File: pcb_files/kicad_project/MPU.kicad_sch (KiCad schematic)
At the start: 4 parts, among them U5 MPU-6500

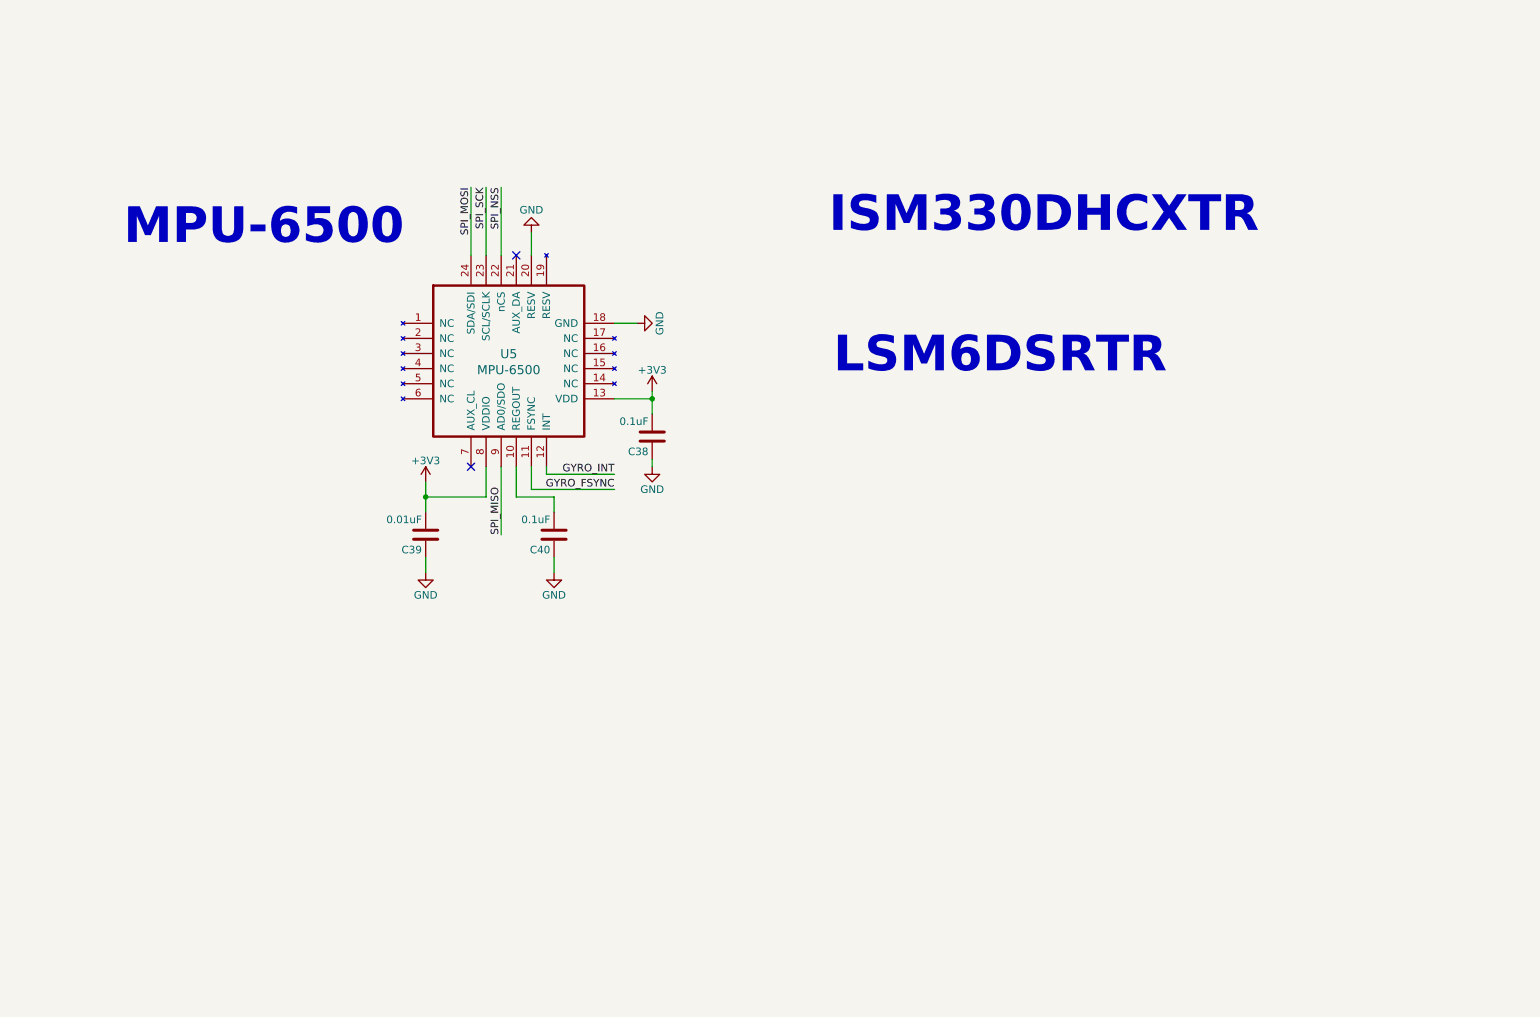
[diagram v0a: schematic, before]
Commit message: Añade nuevo MPU LSM6DSR
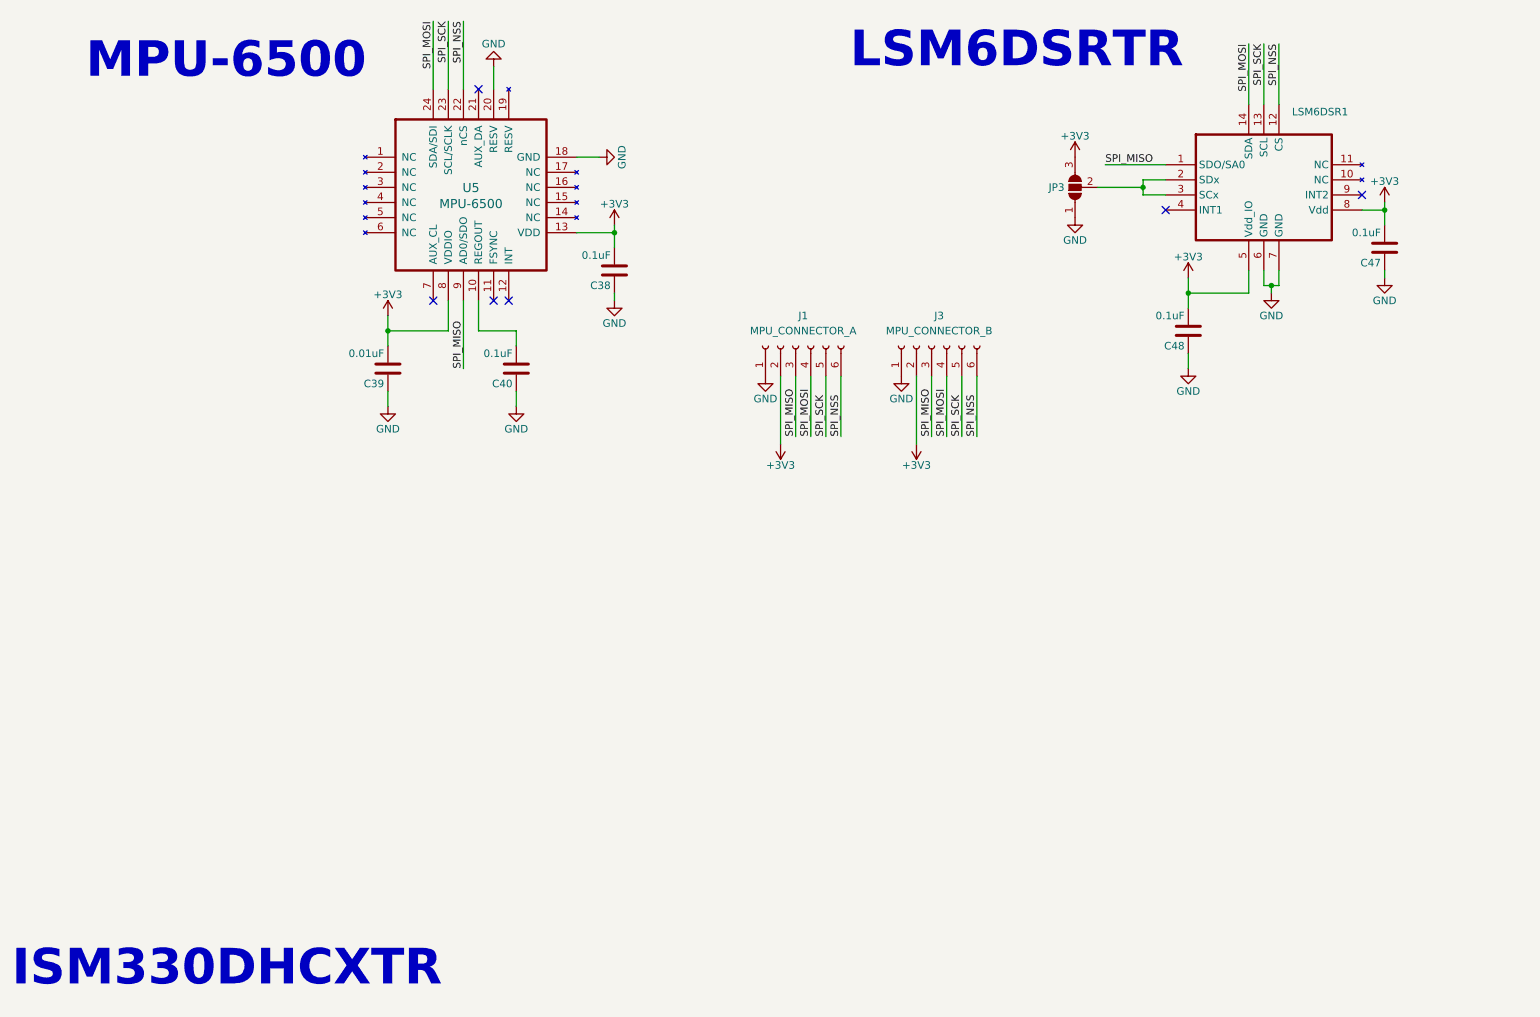
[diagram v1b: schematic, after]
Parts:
- added C47, C48: 0.1uF, Capacitor_SMD:C_0805_2012Metric, symbol Device:C
- added J1: MPU_CONNECTOR_A, symbol Connector:Conn_01x06_Socket
- added J3: MPU_CONNECTOR_B, symbol Connector:Conn_01x06_Socket
- added JP3: SolderJumper_3_Open, symbol Jumper:SolderJumper_3_Open
- added LSM6DSR1: ~, symbol custom_symbols:LSM6DSR
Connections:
- net +3V3: now also C47.2, C48.2, J1.2 (Pin_2), J3.2 (Pin_2), JP3.3 (B), LSM6DSR1.5 (Vdd_IO), LSM6DSR1.8 (Vdd)
- net GND: now also C47.1, C48.1, J1.1 (Pin_1), J3.1 (Pin_1), JP3.1 (A), LSM6DSR1.6 (GND), LSM6DSR1.7 (GND)
- net SPI_MISO: now also J1.3 (Pin_3), J3.3 (Pin_3), LSM6DSR1.1 (SDO/SA0)
- net SPI_MOSI: now also J1.4 (Pin_4), J3.4 (Pin_4), LSM6DSR1.14 (SDA)
- net SPI_NSS: now also J1.6 (Pin_6), J3.6 (Pin_6), LSM6DSR1.12 (CS)
- net SPI_SCK: now also J1.5 (Pin_5), J3.5 (Pin_5), LSM6DSR1.13 (SCL)
- net GYRO_FSYNC: no longer names the net of U5.11 (FSYNC)
- net GYRO_INT: no longer names the net of U5.12 (INT)
- new net: JP3.2 (C), LSM6DSR1.2 (SDx), LSM6DSR1.3 (SCx)
- no-connect marks 2 -> 6
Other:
- moved on the sheet: C38, C39, C40, U5

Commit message: Finaliza (En principio) el esquematico
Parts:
- removed J1: MPU_CONNECTOR_A, symbol Connector:Conn_01x06_Socket
- removed J3: MPU_CONNECTOR_B, symbol Connector:Conn_01x06_Socket
- added DATA_MPU1, DATA_MPU2: Conn_01x04_Socket, symbol Connector:Conn_01x04_Socket
- added POWER_MPU1, POWER_MPU2: Conn_01x02_Socket, symbol Connector:Conn_01x02_Socket
- renumbered C39 to C34, C40 to C35, C38 to C36, C48 to C37, C47 to C38, JP3 to JP2, U5 to U2
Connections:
- net +3V3 renamed 3.3_MPU
- net 3.3_MPU: now also POWER_MPU1.2 (Pin_2), POWER_MPU2.2 (Pin_2)
- net GND renamed GND_MPU
- net GND_MPU: now also POWER_MPU1.1 (Pin_1), POWER_MPU2.1 (Pin_1)
- net SPI_MISO renamed SPI_MISO_CONN
- net SPI_MISO_CONN: now also DATA_MPU1.1 (Pin_1), DATA_MPU2.1 (Pin_1)
- net SPI_MOSI renamed SPI_MOSI_CONN
- net SPI_MOSI_CONN: now also DATA_MPU1.2 (Pin_2), DATA_MPU2.2 (Pin_2)
- net SPI_NSS renamed SPI_NSS_CONN
- net SPI_NSS_CONN: now also DATA_MPU1.4 (Pin_4), DATA_MPU2.4 (Pin_4)
- net SPI_SCK renamed SPI_SCK_CONN
- net SPI_SCK_CONN: now also DATA_MPU1.3 (Pin_3), DATA_MPU2.3 (Pin_3)
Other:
- note added: "MPUs"
- moved on the sheet: C34, C35, C36, C37, C38, JP2, LSM6DSR1, U2

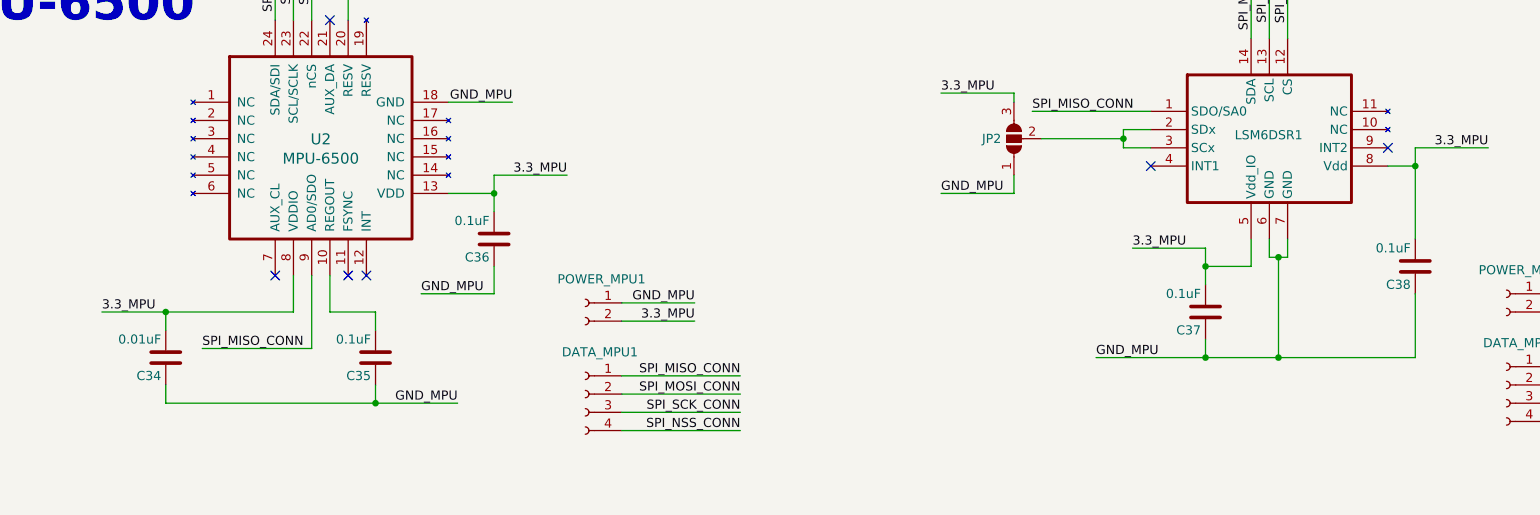
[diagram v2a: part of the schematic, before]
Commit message: Correlaciona toda la NetList, añade EdgeCuts y comienza el posicionamiento de componentes
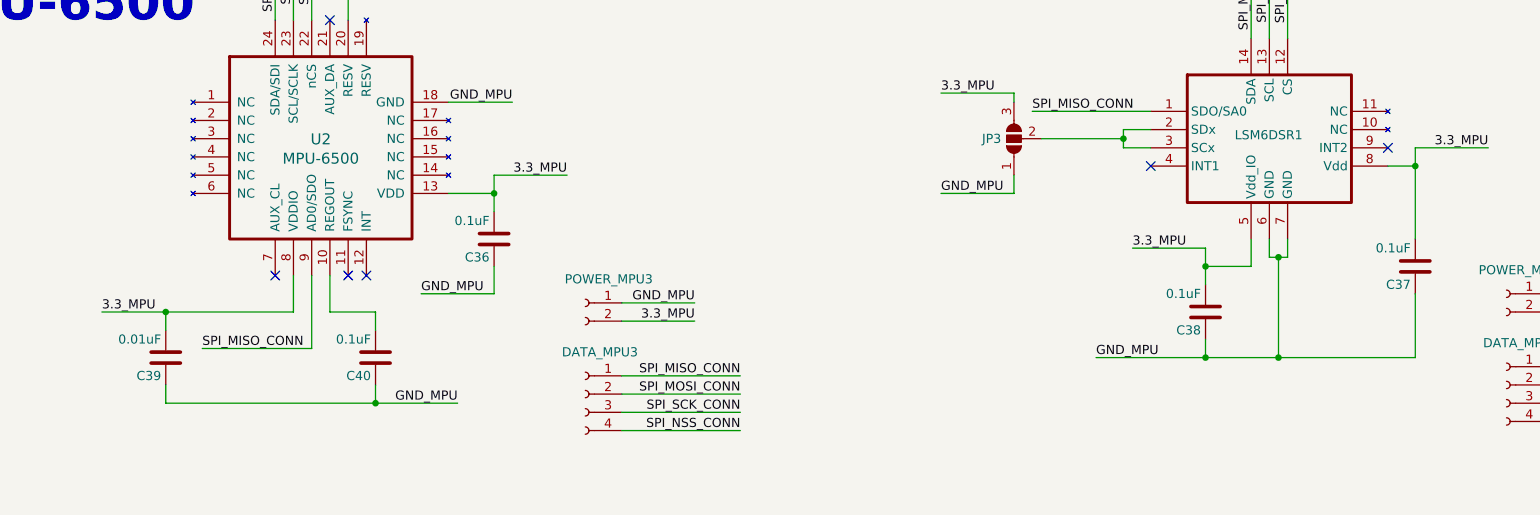
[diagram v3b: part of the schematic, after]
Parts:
- C36: footprint Capacitor_SMD:C_0805_2012Metric -> Capacitor_SMD:C_0402_1005Metric_Pad0.74x0.62mm_HandSolder
- C37: renamed from C38; footprint Capacitor_SMD:C_0805_2012Metric -> Capacitor_SMD:C_0402_1005Metric_Pad0.74x0.62mm_HandSolder
- C38: renamed from C37; footprint Capacitor_SMD:C_0805_2012Metric -> Capacitor_SMD:C_0402_1005Metric_Pad0.74x0.62mm_HandSolder
- C39: renamed from C34; footprint Capacitor_SMD:C_0805_2012Metric -> Capacitor_SMD:C_0402_1005Metric_Pad0.74x0.62mm_HandSolder
- C40: renamed from C35; footprint Capacitor_SMD:C_0805_2012Metric -> Capacitor_SMD:C_0402_1005Metric_Pad0.74x0.62mm_HandSolder
- DATA_MPU2, POWER_MPU2: footprint (none) -> custom_footprints:1x05 Pad
- DATA_MPU3: renamed from DATA_MPU1; footprint (none) -> custom_footprints:1x05 Pad
- JP3: renamed from JP2; footprint (none) -> Jumper:SolderJumper-3_P1.3mm_Open_RoundedPad1.0x1.5mm
- LSM6DSR1: footprint (none) -> Sensor_Motion:Analog_LGA-16_3.25x3mm_P0.5mm_LayoutBorder3x5y
- POWER_MPU3: renamed from POWER_MPU1; footprint (none) -> custom_footprints:1x05 Pad
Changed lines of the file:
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@@
 			)
 		)
-		(property "Footprint" ""
+		(property "Footprint" "Sensor_Motion:Analog_LGA-16_3.25x3mm_P0.5mm_LayoutBorder3x5y"
 			(at 215.9 93.98 0)
 			(effects
@@
 		(on_board yes)
 		(dnp no)
-		(property "Reference" "C38"
+		(property "Reference" "C37"
 			(at 235.585 113.03 0)
 			(effects
@@
 			)
 		)
-		(property "Footprint" "Capacitor_SMD:C_0805_2012Metric"
+		(property "Footprint" "Capacitor_SMD:C_0402_1005Metric_Pad0.74x0.62mm_HandSolder"
 			(at 235.2548 106.68 0)
 			(effects
@@
 			(project "ZoroBot3"
 				(path "/38e8b839-c362-4120-bbf7-582efa82e48d/9d49d3a6-8e33-4528-aef9-1bba3efb9fbc"
-					(reference "C38")
+					(reference "C37")
 					(unit 1)
 				)
@@
 		(on_board yes)
 		(dnp no)
-		(property "Reference" "POWER_MPU1"
-			(at 129.032 112.268 0)
+		(property "Reference" "POWER_MPU3"
+			(at 130.048 112.268 0)
 			(effects
 				(font
@@
 			)
 		)
-		(property "Footprint" ""
+		(property "Footprint" "custom_footprints:1x05 Pad"
 			(at 120.65 115.57 0)
 			(effects
@@
 			(project "ZoroBot3"
 				(path "/38e8b839-c362-4120-bbf7-582efa82e48d/9d49d3a6-8e33-4528-aef9-1bba3efb9fbc"
-					(reference "POWER_MPU1")
+					(reference "POWER_MPU3")
 					(unit 1)
 				)
@@
 			)
 		)
-		(property "Footprint" ""
+		(property "Footprint" "custom_footprints:1x05 Pad"
 			(at 248.92 127 0)
 			(effects
@@
 			)
 		)
-		(property "Footprint" "Capacitor_SMD:C_0805_2012Metric"
+		(property "Footprint" "Capacitor_SMD:C_0402_1005Metric_Pad0.74x0.62mm_HandSolder"
 			(at 106.9848 102.87 0)
 			(effects
@@
 		(on_board yes)
 		(dnp no)
-		(property "Reference" "C34"
+		(property "Reference" "C39"
 			(at 61.595 125.73 0)
 			(effects
@@
 			)
 		)
-		(property "Footprint" "Capacitor_SMD:C_0805_2012Metric"
+		(property "Footprint" "Capacitor_SMD:C_0402_1005Metric_Pad0.74x0.62mm_HandSolder"
 			(at 61.2648 119.38 0)
 			(effects
@@
 			(project "ZoroBot3"
 				(path "/38e8b839-c362-4120-bbf7-582efa82e48d/9d49d3a6-8e33-4528-aef9-1bba3efb9fbc"
-					(reference "C34")
+					(reference "C39")
 					(unit 1)
 				)
@@
 		(on_board yes)
 		(dnp no)
-		(property "Reference" "DATA_MPU1"
+		(property "Reference" "DATA_MPU3"
 			(at 122.682 122.428 0)
 			(effects
@@
 			)
 		)
-		(property "Footprint" ""
+		(property "Footprint" "custom_footprints:1x05 Pad"
 			(at 120.65 128.27 0)
 			(effects
@@
 			(project "ZoroBot3"
 				(path "/38e8b839-c362-4120-bbf7-582efa82e48d/9d49d3a6-8e33-4528-aef9-1bba3efb9fbc"
-					(reference "DATA_MPU1")
+					(reference "DATA_MPU3")
 					(unit 1)
 				)
@@
 		(on_board yes)
 		(dnp no)
-		(property "Reference" "C35"
+		(property "Reference" "C40"
 			(at 90.805 125.73 0)
 			(effects
@@
 			)
 		)
-		(property "Footprint" "Capacitor_SMD:C_0805_2012Metric"
+		(property "Footprint" "Capacitor_SMD:C_0402_1005Metric_Pad0.74x0.62mm_HandSolder"
 			(at 90.4748 119.38 0)
 			(effects
@@
 			(project "ZoroBot3"
 				(path "/38e8b839-c362-4120-bbf7-582efa82e48d/9d49d3a6-8e33-4528-aef9-1bba3efb9fbc"
-					(reference "C35")
+					(reference "C40")
 					(unit 1)
 				)
@@
 		(on_board yes)
 		(dnp no)
-		(property "Reference" "C37"
+		(property "Reference" "C38"
 			(at 206.375 119.38 0)
 			(effects
@@
 			)
 		)
-		(property "Footprint" "Capacitor_SMD:C_0805_2012Metric"
+		(property "Footprint" "Capacitor_SMD:C_0402_1005Metric_Pad0.74x0.62mm_HandSolder"
 			(at 206.0448 113.03 0)
 			(effects
@@
 			(project "ZoroBot3"
 				(path "/38e8b839-c362-4120-bbf7-582efa82e48d/9d49d3a6-8e33-4528-aef9-1bba3efb9fbc"
-					(reference "C37")
+					(reference "C38")
 					(unit 1)
 				)
@@
 		(on_board yes)
 		(dnp no)
-		(property "Reference" "JP2"
+		(property "Reference" "JP3"
 			(at 178.562 92.71 90)
 			(effects
@@
 			)
 		)
-		(property "Footprint" ""
+		(property "Footprint" "Jumper:SolderJumper-3_P1.3mm_Open_RoundedPad1.0x1.5mm"
 			(at 180.34 92.71 0)
 			(effects
@@
 			(project "ZoroBot3"
 				(path "/38e8b839-c362-4120-bbf7-582efa82e48d/9d49d3a6-8e33-4528-aef9-1bba3efb9fbc"
-					(reference "JP2")
+					(reference "JP3")
 					(unit 1)
 				)
@@
 			)
 		)
-		(property "Footprint" ""
+		(property "Footprint" "custom_footprints:1x05 Pad"
 			(at 248.92 114.3 0)
 			(effects
